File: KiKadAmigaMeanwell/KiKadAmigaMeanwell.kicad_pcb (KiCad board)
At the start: 2 copper layers, 99 x 148.5 mm, 8 parts

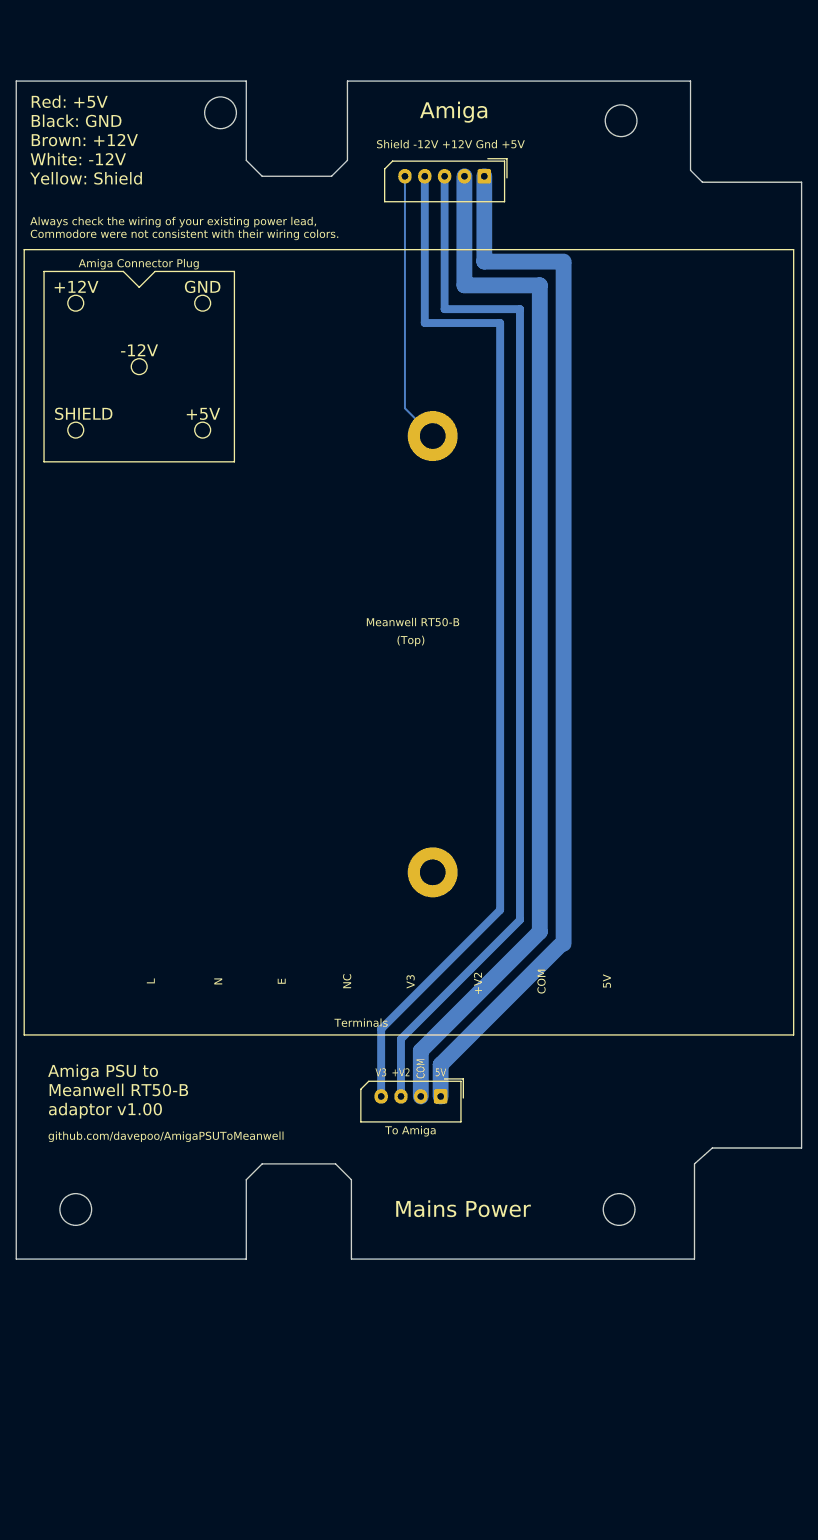
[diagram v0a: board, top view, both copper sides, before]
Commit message: - changing out the connectors to Molex KK 5 pin connectors / adding 5V/12V fan headers (not connected yet)
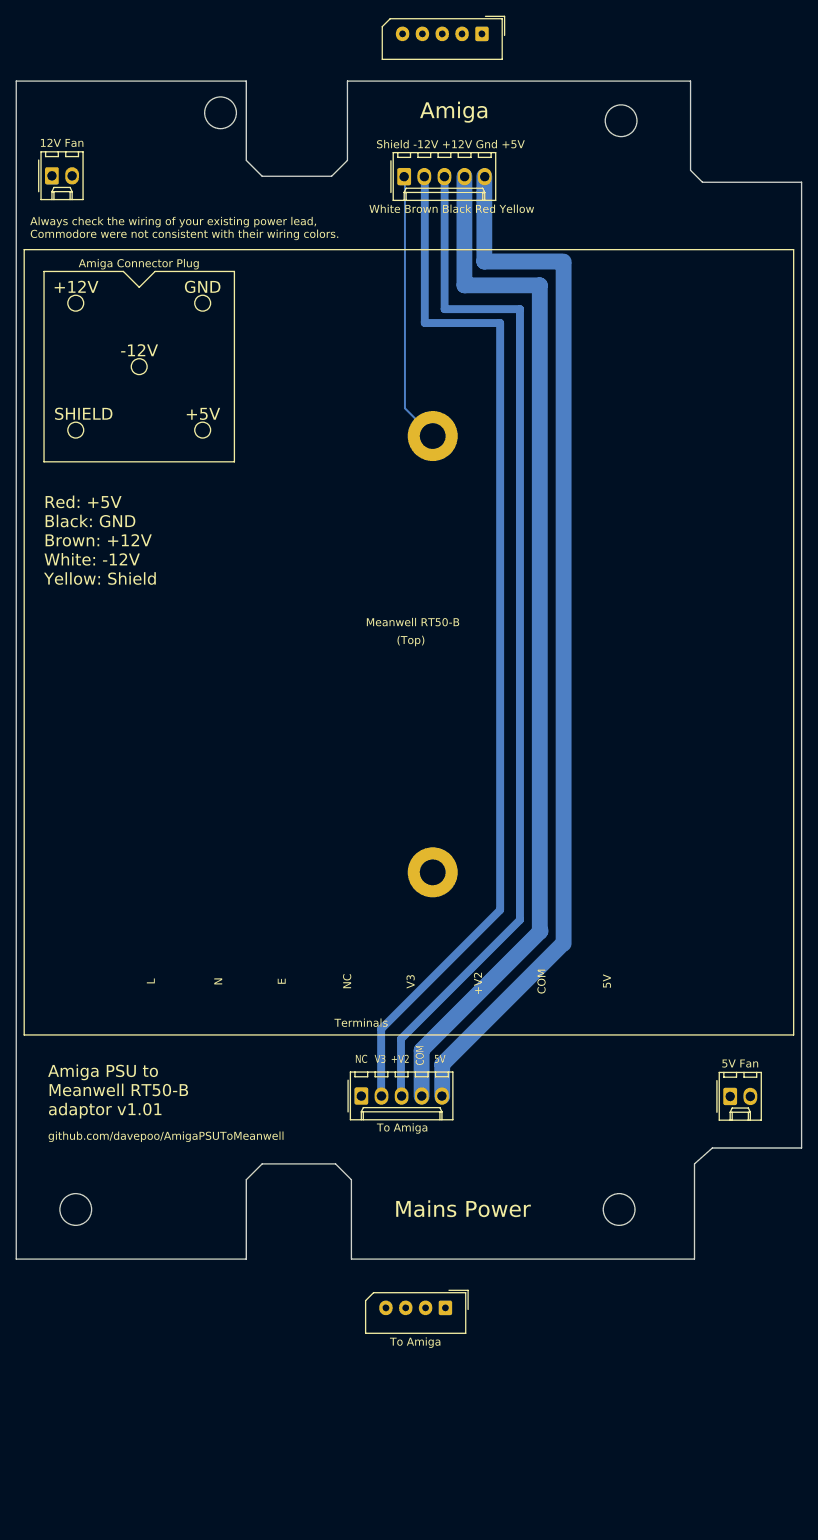
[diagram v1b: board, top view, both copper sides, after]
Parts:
- added 12V Fan: Molex_KK-254_AE-6410-02A_1x02_P2.54mm_Vertical, Connector_Molex:Molex_KK-254_AE-6410-02A_1x02_P2.54mm_Vertical, F.Cu at (73.0, 45.2)
- added 5V Fan: Molex_KK-254_AE-6410-02A_1x02_P2.54mm_Vertical, Connector_Molex:Molex_KK-254_AE-6410-02A_1x02_P2.54mm_Vertical, F.Cu at (158.5, 161.2)
- added To Amiga: Molex_KK-254_AE-6410-05A_1x05_P2.54mm_Vertical, Connector_Molex:Molex_KK-254_AE-6410-05A_1x05_P2.54mm_Vertical, F.Cu at (112.0, 161.2)
- added White Brown Black Red Yellow: Molex_KK-254_AE-6410-05A_1x05_P2.54mm_Vertical, Connector_Molex:Molex_KK-254_AE-6410-05A_1x05_P2.54mm_Vertical, F.Cu at (117.4, 45.3)
- moved To Amiga 26.7 mm to (122.6, 187.9)
- moved White Brown Black Red Yellow 18.0 mm to (127.2, 27.3)
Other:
- board text added: "Amiga PSU to Meanwell RT50-B adaptor v1.01"
- board text added: "NC"
- board text removed: "Amiga PSU to Meanwell RT50-B adaptor v1.00"

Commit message: - adding schematic, and routing the tracks for the connectors and fan headers on the PCB
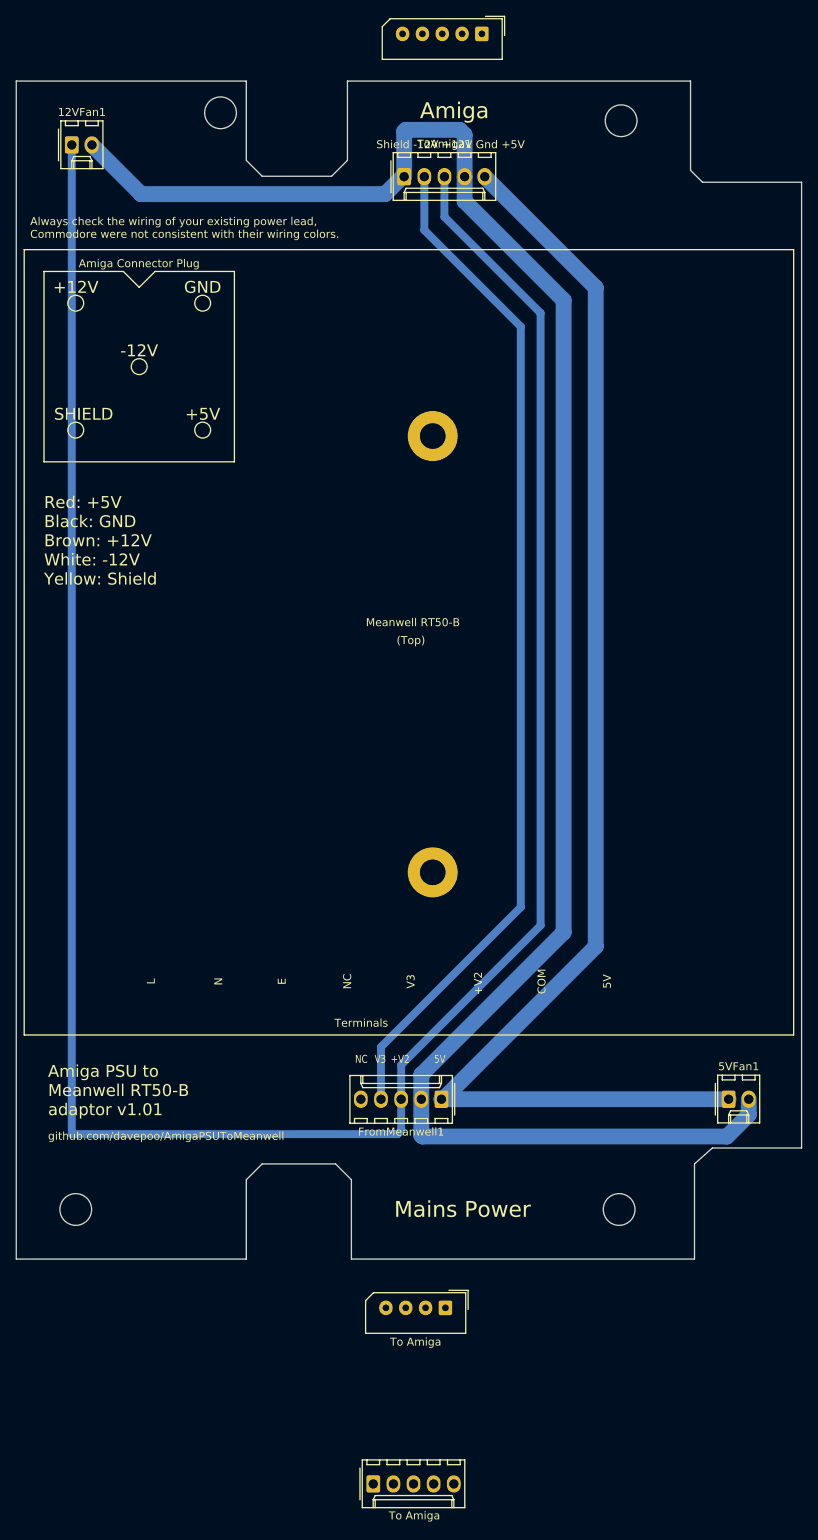
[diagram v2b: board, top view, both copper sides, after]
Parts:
- removed 12V Fan: Molex_KK-254_AE-6410-02A_1x02_P2.54mm_Vertical, Connector_Molex:Molex_KK-254_AE-6410-02A_1x02_P2.54mm_Vertical
- removed 5V Fan: Molex_KK-254_AE-6410-02A_1x02_P2.54mm_Vertical, Connector_Molex:Molex_KK-254_AE-6410-02A_1x02_P2.54mm_Vertical
- removed the White Brown Black Red Yellow at (117.4, 45.3)
- added 12VFan1: Conn_01x02, Connector_Molex:Molex_KK-254_AE-6410-02A_1x02_P2.54mm_Vertical, F.Cu at (75.5, 41.3)
- added 5VFan1: Conn_01x02, Connector_Molex:Molex_KK-254_AE-6410-02A_1x02_P2.54mm_Vertical, F.Cu at (158.3, 161.6)
- added FromMeanwell1: Conn_01x05, Connector_Molex:Molex_KK-254_AE-6410-05A_1x05_P2.54mm_Vertical, F.Cu at (122.1, 161.6)
- added ToAmiga1: Conn_01x05, Connector_Molex:Molex_KK-254_AE-6410-05A_1x05_P2.54mm_Vertical, F.Cu at (117.4, 45.3)
- moved To Amiga 48.9 mm to (113.5, 210.1)
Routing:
- net (no net): track 562.1 -> 0.00 mm
- net +12V: track 0.00 -> 299.0 mm
- net GND: track 0.00 -> 239.7 mm
- net +5V: track 0.00 -> 166.5 mm
- net -12V: track 0.00 -> 128.6 mm
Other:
- net class 0.5A added: clearance 0.2, trace_width 1, via_dia 0.8, via_drill 0.4
- net class 2A added: clearance 0.2, trace_width 1, via_dia 0.8, via_drill 0.4
- net class 4A added: clearance 0.2, trace_width 2, via_dia 0.8, via_drill 0.4
- board text removed: "COM"

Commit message: - connecting the shield pin to earth instead of ground, making smaller trace widths for the fan headers (0.5A)
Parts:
- removed the To Amiga at (113.5, 210.1)
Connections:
- Meanwell RT50-B pad : (no net) -> Earth
- ToAmiga1 pad 1: GND -> Earth
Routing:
- net +12V: track 299.0 -> 190.9 mm
- net Earth: track 0.00 -> 34.2 mm
- net GND: track 239.7 -> 241.0 mm

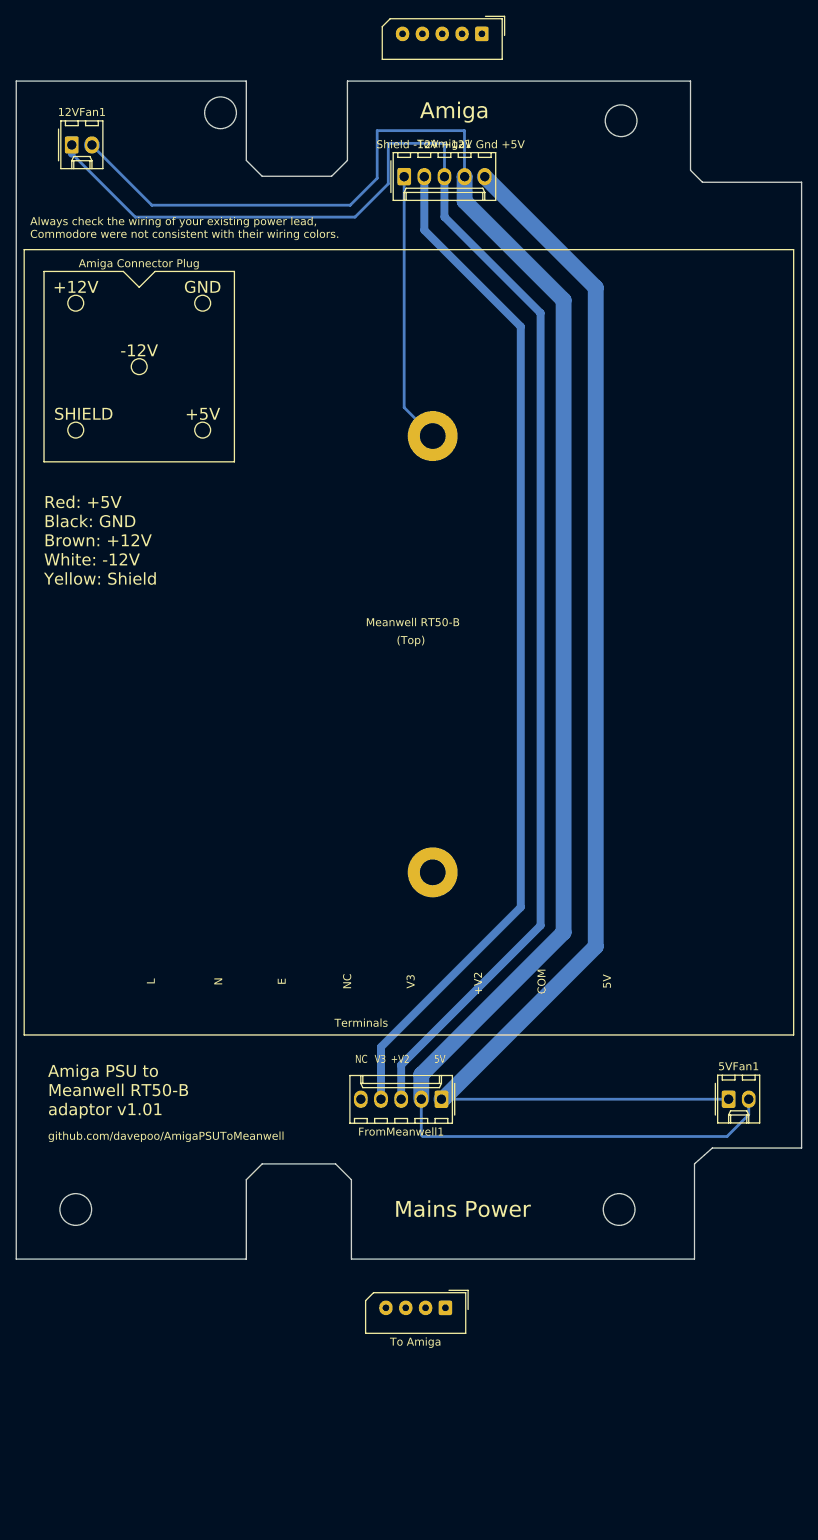
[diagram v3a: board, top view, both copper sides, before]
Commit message: - adding a second 5V fan header
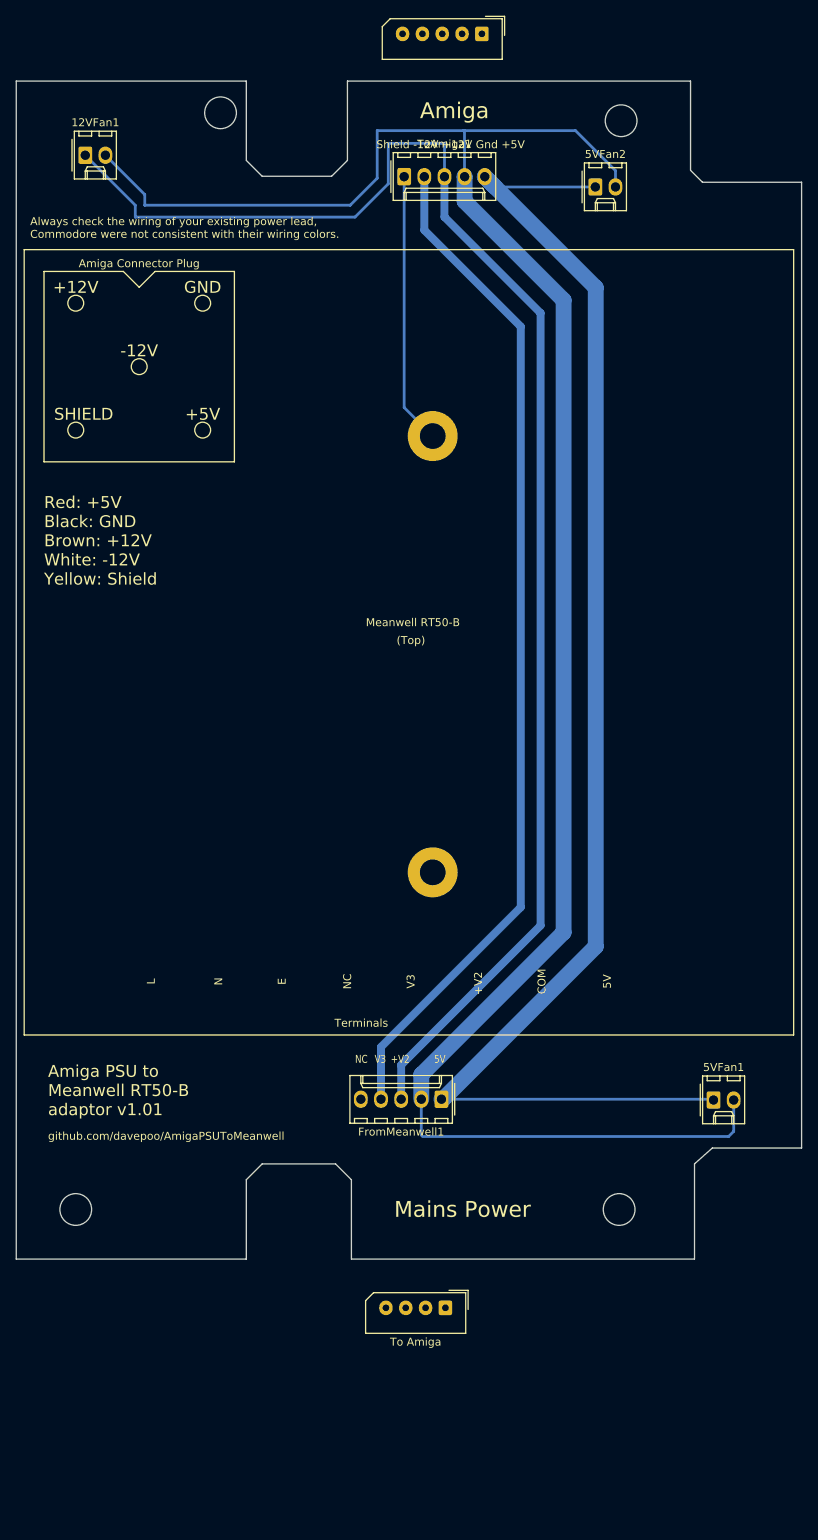
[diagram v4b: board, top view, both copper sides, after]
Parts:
- added 5VFan2: Conn_01x02, Connector_Molex:Molex_KK-254_AE-6410-02A_1x02_P2.54mm_Vertical, F.Cu at (141.5, 46.6)
- moved 12VFan1 2.14 mm to (77.2, 42.6)
- moved 5VFan1 1.90 mm to (156.4, 161.7)
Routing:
- net GND: track 241.0 -> 263.1 mm
- net +5V: track 166.5 -> 178.9 mm
- net +12V: track 190.9 -> 188.9 mm

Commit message: - adjusting edge cuts to fit around the plastic standoffs
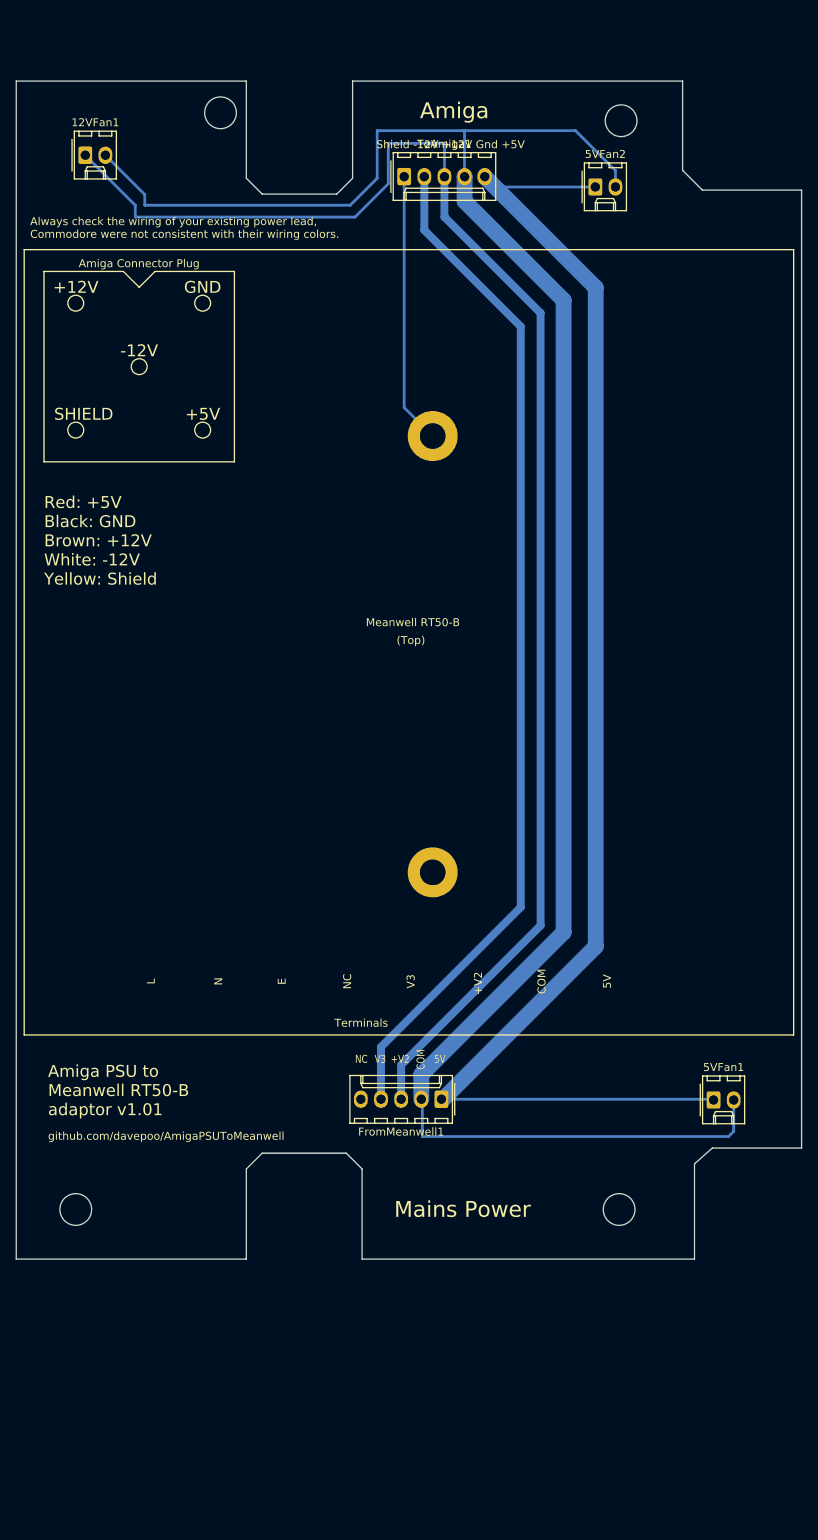
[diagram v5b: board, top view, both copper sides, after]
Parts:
- removed To Amiga: Molex_SPOX_5267-04A_1x04_P2.50mm_Vertical, Connector_Molex:Molex_SPOX_5267-04A_1x04_P2.50mm_Vertical
- removed White Brown Black Red Yellow: Molex_SPOX_5267-05A_1x05_P2.50mm_Vertical, Connector_Molex:Molex_SPOX_5267-05A_1x05_P2.50mm_Vertical
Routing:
- net +5V: track 178.9 -> 176.9 mm
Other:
- outline, holes or cut-outs redrawn
- board text added: "COM"

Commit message: - adding voltage and ground silkscreen to the fan headers
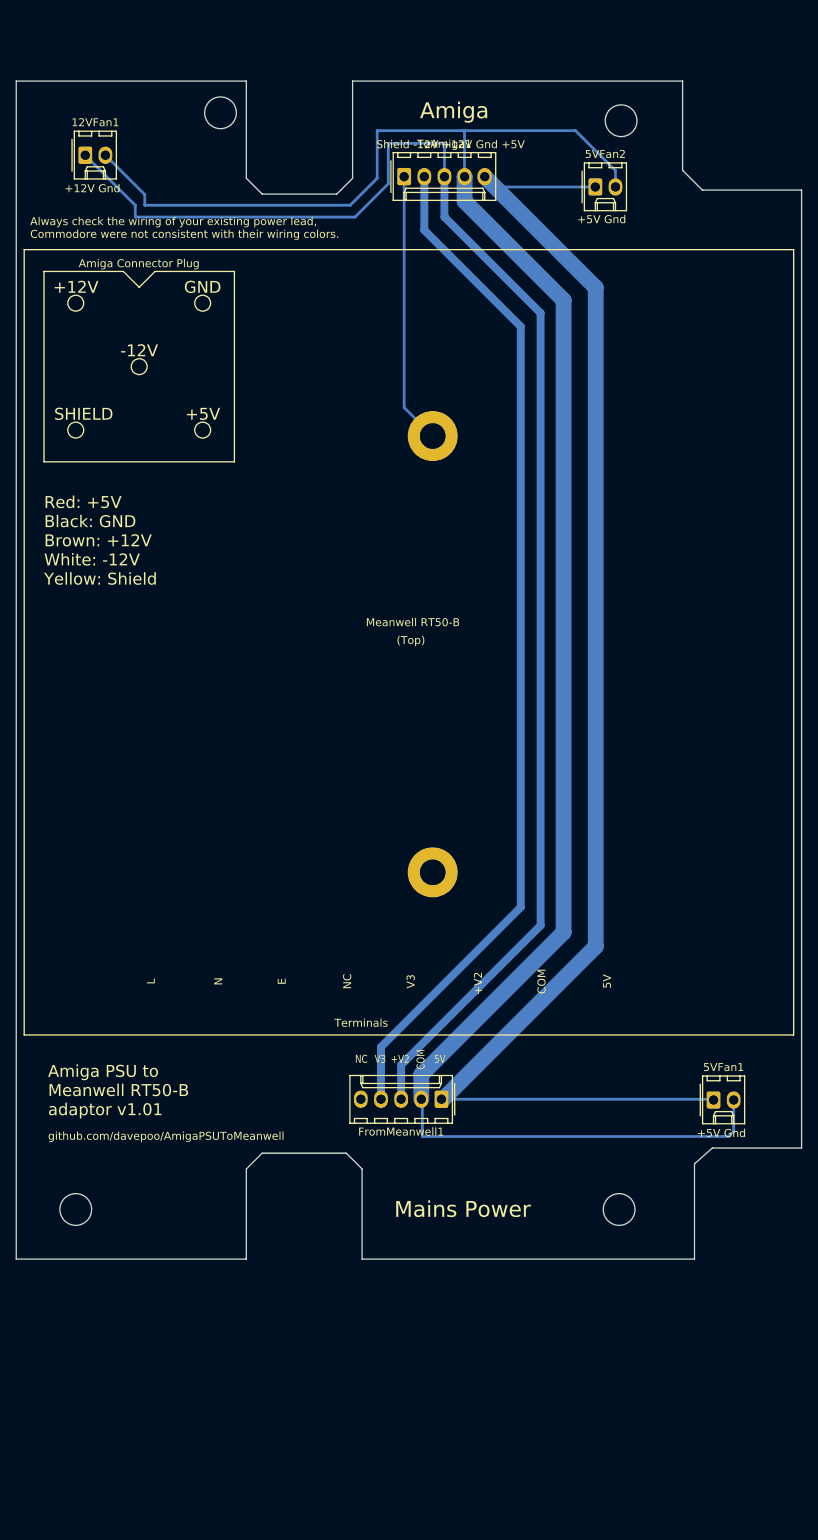
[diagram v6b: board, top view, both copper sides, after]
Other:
- board text added: "+12V Gnd"
- board text added: "+5V Gnd"
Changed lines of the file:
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@@
   (general
     (thickness 1.6)
-    (drawings 38)
+    (drawings 41)
     (tracks 47)
     (zones 0)
@@
     (pad 1 np_thru_hole circle (at 0 0 180) (size 4 4) (drill 4) (layers *.Cu *.Mask))
   )
+  (gr_text "+12V Gnd" (at 78.1 46.8) (layer F.SilkS)
+    (effects (font (size 1 1) (thickness 0.15)))
+  )
+  (gr_text "+5V Gnd" (at 157.4 165.9) (layer F.SilkS)
+    (effects (font (size 1 1) (thickness 0.15)))
+  )
+  (gr_text "+5V Gnd" (at 142.3 50.7) (layer F.SilkS)
+    (effects (font (size 1 1) (thickness 0.15)))
+  )
   (gr_text COM (at 119.5 156.6 90) (layer F.SilkS)
